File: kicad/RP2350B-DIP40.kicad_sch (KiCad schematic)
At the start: 30 parts, among them J1 USB_C_Receptacle_USB2.0_16P, J2 Conn_ARM_JTAG_SWD_10, J3 Conn_01x03_Socket, J4 qwiic, J5 Micro_SD_Card, U1 TPD2EUSB30, U2 Picossci_B2_RB2350B, U3 18F47Q43, U4 TPS22917DBV

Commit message: Add PCB design RP2350B-DIP40-rev1.0
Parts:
- removed J2: Conn_ARM_JTAG_SWD_10, Connector_PinHeader_1.27mm:PinHeader_2x05_P1.27mm_Vertical_SMD, symbol Connector:Conn_ARM_JTAG_SWD_10
- removed J3: Conn_01x03_Socket, Connector_JST:JST_SH_SM03B-SRSS-TB_1x03-1MP_P1.00mm_Horizontal, symbol Connector:Conn_01x03_Socket
- removed TP1: TestPoint, TestPoint:TestPoint_Pad_1.0x1.0mm, symbol Connector:TestPoint
- added J2: debug connector, Connector_JST:JST_SH_SM03B-SRSS-TB_1x03-1MP_P1.00mm_Horizontal, symbol Library:Raspi_debug_swd_conn
- added J3: uart connector, Connector_JST:JST_SH_SM03B-SRSS-TB_1x03-1MP_P1.00mm_Horizontal, symbol Library:Raspi_debug_uart_conn
- R4: value 10K -> 33R
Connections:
- net SWO is gone; now on net RD2: U2.32 (GP26)
- net nRESET is gone; now on net UART0_TX: R4.2
- net +3.3V: no longer R4.1
- net 5V_OUT_EN: now also U2.41 (GP35); no longer U2.33 (GP27)
- net GND: now also J2.2 (GND), J3.2 (GND)
- net MISO: now also U2.47 (GP40(AIN0)); no longer U2.8 (GP4)
- net MOSI: now also U2.50 (GP43(AIN3)); no longer U2.11 (GP7)
- net RB0: now also U2.4 (GP0); no longer U2.47 (GP40(AIN0))
- net RB1: now also U2.5 (GP1); no longer U2.48 (GP41(AIN1))
- net RB2: now also U2.6 (GP2); no longer U2.49 (GP42(AIN2))
- net RB3: now also U2.7 (GP3); no longer U2.50 (GP43(AIN3))
- net RB4: now also U2.8 (GP4); no longer U2.51 (GP44(AIN4))
- net RB5: now also U2.9 (GP5); no longer U2.52 (GP45(AIN5))
- net RB6: now also U2.10 (GP6); no longer U2.53 (GP46(AIN6))
- net RB7: now also U2.11 (GP7); no longer U2.54 (GP47(AIN7))
- net RD0: now also U2.30 (GP24(LED1)); no longer U2.38 (GP32)
- net RD1: now also U2.31 (GP25(LED2)); no longer U2.39 (GP33)
- net RD2: no longer U2.40 (GP34)
- net RD3: now also U2.33 (GP27); no longer U2.41 (GP35)
- net RD4: now also U2.34 (GP28); no longer U2.42 (GP36)
- net RD5: now also U2.35 (GP29); no longer U2.43 (GP37)
- net RD6: now also U2.36 (GP30); no longer U2.44 (GP38)
- net RD7: now also U2.37 (GP31); no longer U2.45 (GP39)
- net RE0: now also U2.42 (GP36); no longer U2.34 (GP28)
- net RE1: now also U2.43 (GP37); no longer U2.35 (GP29)
- net RE2: now also U2.44 (GP38); no longer U2.36 (GP30)
- net RE3: now also U2.45 (GP39); no longer U2.37 (GP31)
- net SCK: now also U2.49 (GP42(AIN2)); no longer U2.10 (GP6)
- net SCL: now also U2.54 (GP47(AIN7)); no longer U2.7 (GP3)
- net SDA: now also U2.53 (GP46(AIN6)); no longer U2.6 (GP2)
- net SPI_CS: now also U2.48 (GP41(AIN1)); no longer U2.9 (GP5)
- net SWCLK: now also J2.1 (SWCLK); no longer R5.1
- net SWDIO: now also J2.3 (SWDIO)
- net UART0_RX: now also R5.2, U2.52 (GP45(AIN5)); no longer U2.5 (GP1)
- net UART0_TX: now also U2.51 (GP44(AIN4)); no longer U2.4 (GP0)
- new net: J3.1 (RX), R5.1
- new net: J3.3 (TX), R4.1

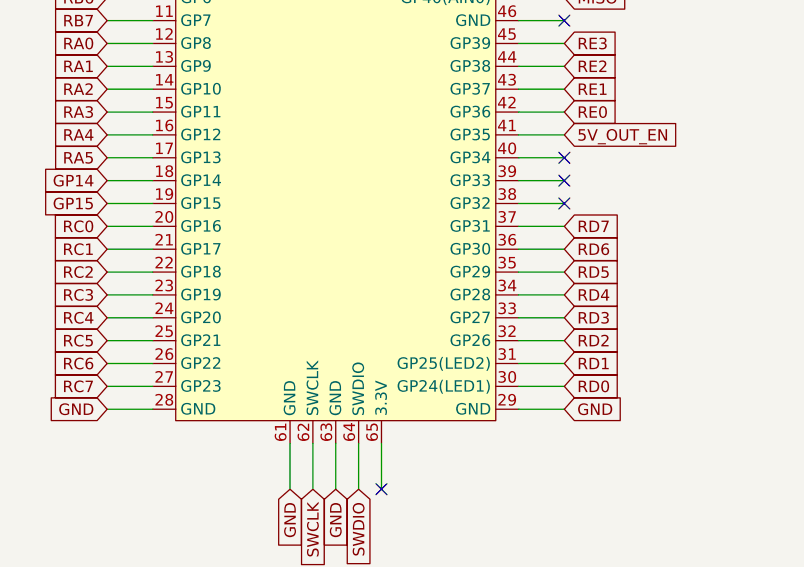
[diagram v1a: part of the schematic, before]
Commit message: Add PCB design RP2350B-DIP40-rev1.1
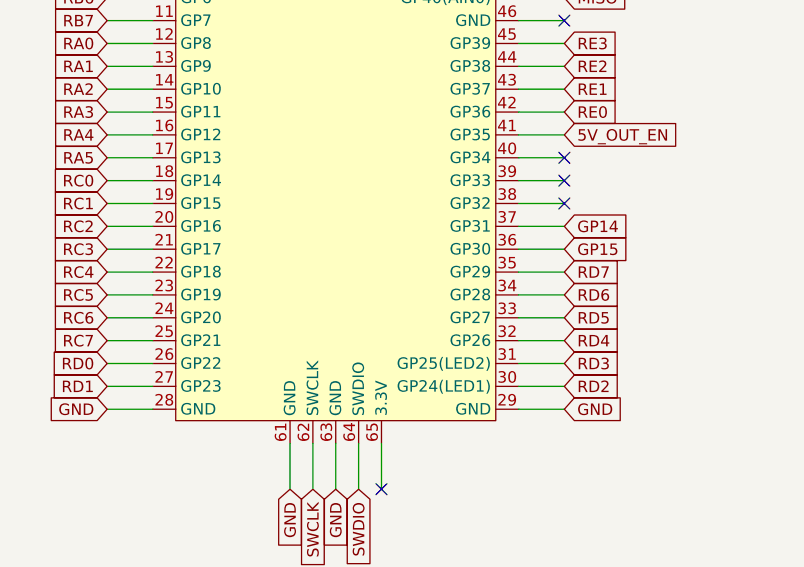
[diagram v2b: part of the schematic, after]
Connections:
- net GP14: now also U2.37 (GP31); no longer U2.18 (GP14)
- net GP15: now also U2.36 (GP30); no longer U2.19 (GP15)
- net RC0: now also U2.18 (GP14); no longer U2.20 (GP16)
- net RC1: now also U2.19 (GP15); no longer U2.21 (GP17)
- net RC2: now also U2.20 (GP16); no longer U2.22 (GP18)
- net RC3: now also U2.21 (GP17); no longer U2.23 (GP19)
- net RC4: now also U2.22 (GP18); no longer U2.24 (GP20)
- net RC5: now also U2.23 (GP19); no longer U2.25 (GP21)
- net RC6: now also U2.24 (GP20); no longer U2.26 (GP22)
- net RC7: now also U2.25 (GP21); no longer U2.27 (GP23)
- net RD0: now also U2.26 (GP22); no longer U2.30 (GP24(LED1))
- net RD1: now also U2.27 (GP23); no longer U2.31 (GP25(LED2))
- net RD2: now also U2.30 (GP24(LED1)); no longer U2.32 (GP26)
- net RD3: now also U2.31 (GP25(LED2)); no longer U2.33 (GP27)
- net RD4: now also U2.32 (GP26); no longer U2.34 (GP28)
- net RD5: now also U2.33 (GP27); no longer U2.35 (GP29)
- net RD6: now also U2.34 (GP28); no longer U2.36 (GP30)
- net RD7: now also U2.35 (GP29); no longer U2.37 (GP31)
